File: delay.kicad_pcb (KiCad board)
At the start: 2 copper layers, 56 parts, among them J1 Footswitch_Terminal_01x02, J2 LED_Socket_01x02, J3 Footswitch_Terminal_Signal_01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, J4 Power_Supply_Terminal_01x02, J5 IO_Ground_Terminal_01x02, U1 L7805, U2 TL072, U3 PT2399

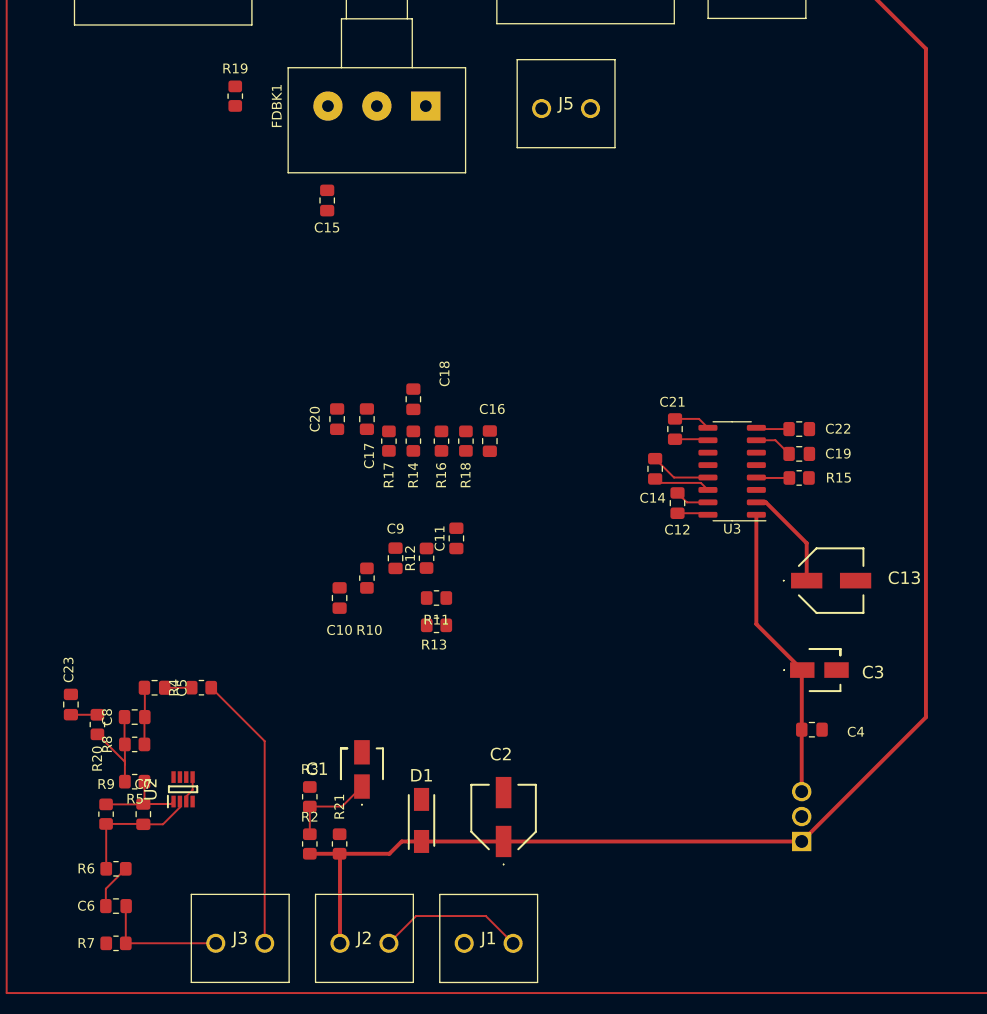
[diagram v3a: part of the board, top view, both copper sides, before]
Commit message: update pcb design schema
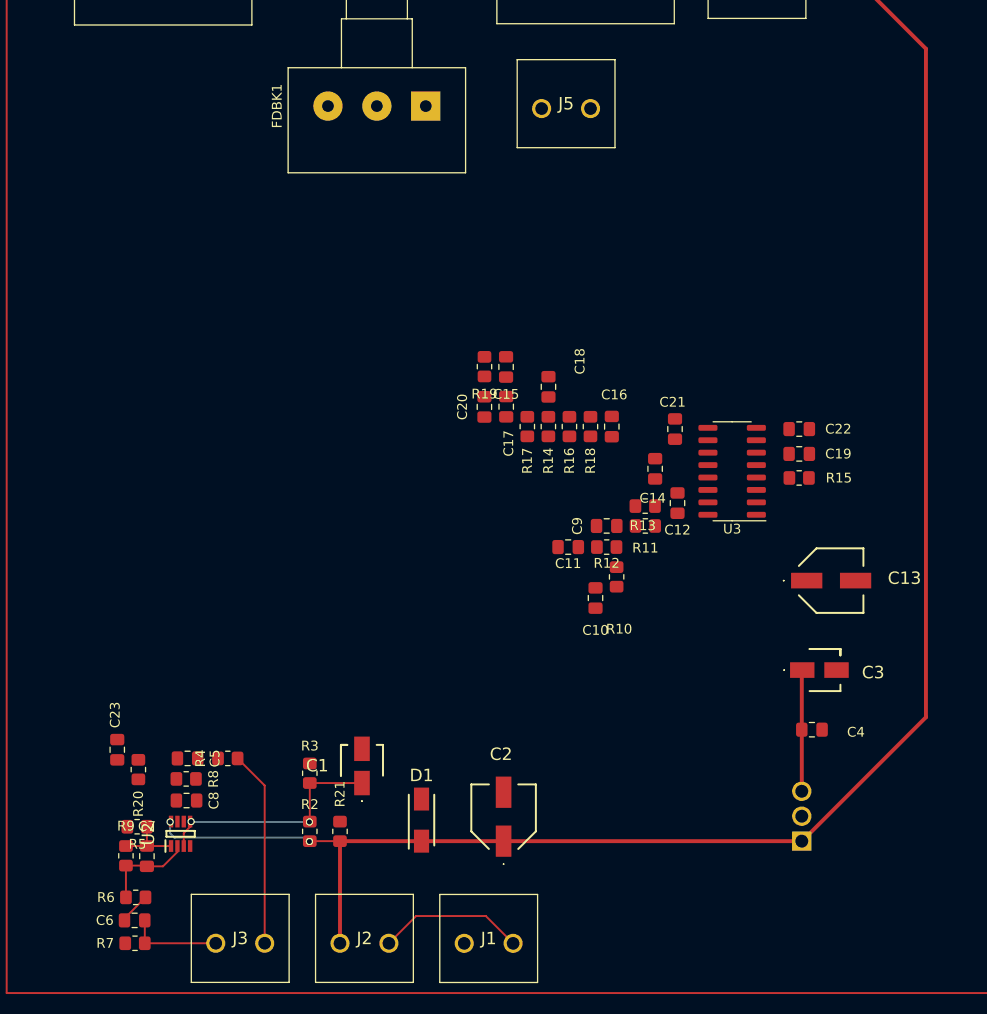
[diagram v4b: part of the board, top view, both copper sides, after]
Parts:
- moved R19 37.6 mm to (169.5, 71.9), turned to -90 degrees
- moved C10 26.2 mm to (180.8, 95.5)
- moved R10 25.5 mm to (183.0, 93.3)
- moved C15 25.0 mm to (171.7, 71.9)
- moved R13 24.6 mm to (185.9, 86.1)
- moved R11 22.6 mm to (185.9, 88.1)
- moved C9 21.8 mm to (182.0, 88.1), turned to 180 degrees
- moved R12 18.5 mm to (182.0, 90.3), turned to 180 degrees
- moved C20 15.1 mm to (169.5, 76.0)
- moved C17 14.3 mm to (171.7, 75.9)
- moved R17 14.2 mm to (173.9, 78.0)
- moved R14 13.9 mm to (176.0, 78.0)
- moved C18 13.9 mm to (176.0, 73.9)
- moved R16 13.2 mm to (178.2, 78.0)
- moved R18 12.8 mm to (180.3, 78.0)
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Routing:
- net /REG_OUT: track 30.3 -> 12.5 mm
- net /+LED: track 155.0 -> 171.5 mm, vias 0 -> 2
- net /V_B: track 12.0 -> 24.2 mm, vias 0 -> 2
- net Net-(U3-REF): track 10.7 -> 0.00 mm
- net Net-(U2B--): track 10.6 -> 0.00 mm
- net /OUTPUT: track 28.4 -> 20.0 mm
- net Net-(U3-LPF2-IN): track 6.20 -> 0.00 mm
- net Net-(C5-Pad1): track 5.89 -> 0.00 mm
- net Net-(U3-LPF2-OUT): track 5.86 -> 0.00 mm
- net Net-(U3-CC1): track 3.92 -> 0.00 mm
- net Net-(U3-OP1-OUT): track 3.74 -> 0.00 mm
- net Net-(U2A--): track 13.5 -> 9.76 mm
- net Net-(U3-LPF1-OUT): track 3.51 -> 0.00 mm
- net /INPUT: track 13.0 -> 9.60 mm
- net Net-(U3-OP1-IN): track 3.41 -> 0.00 mm
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
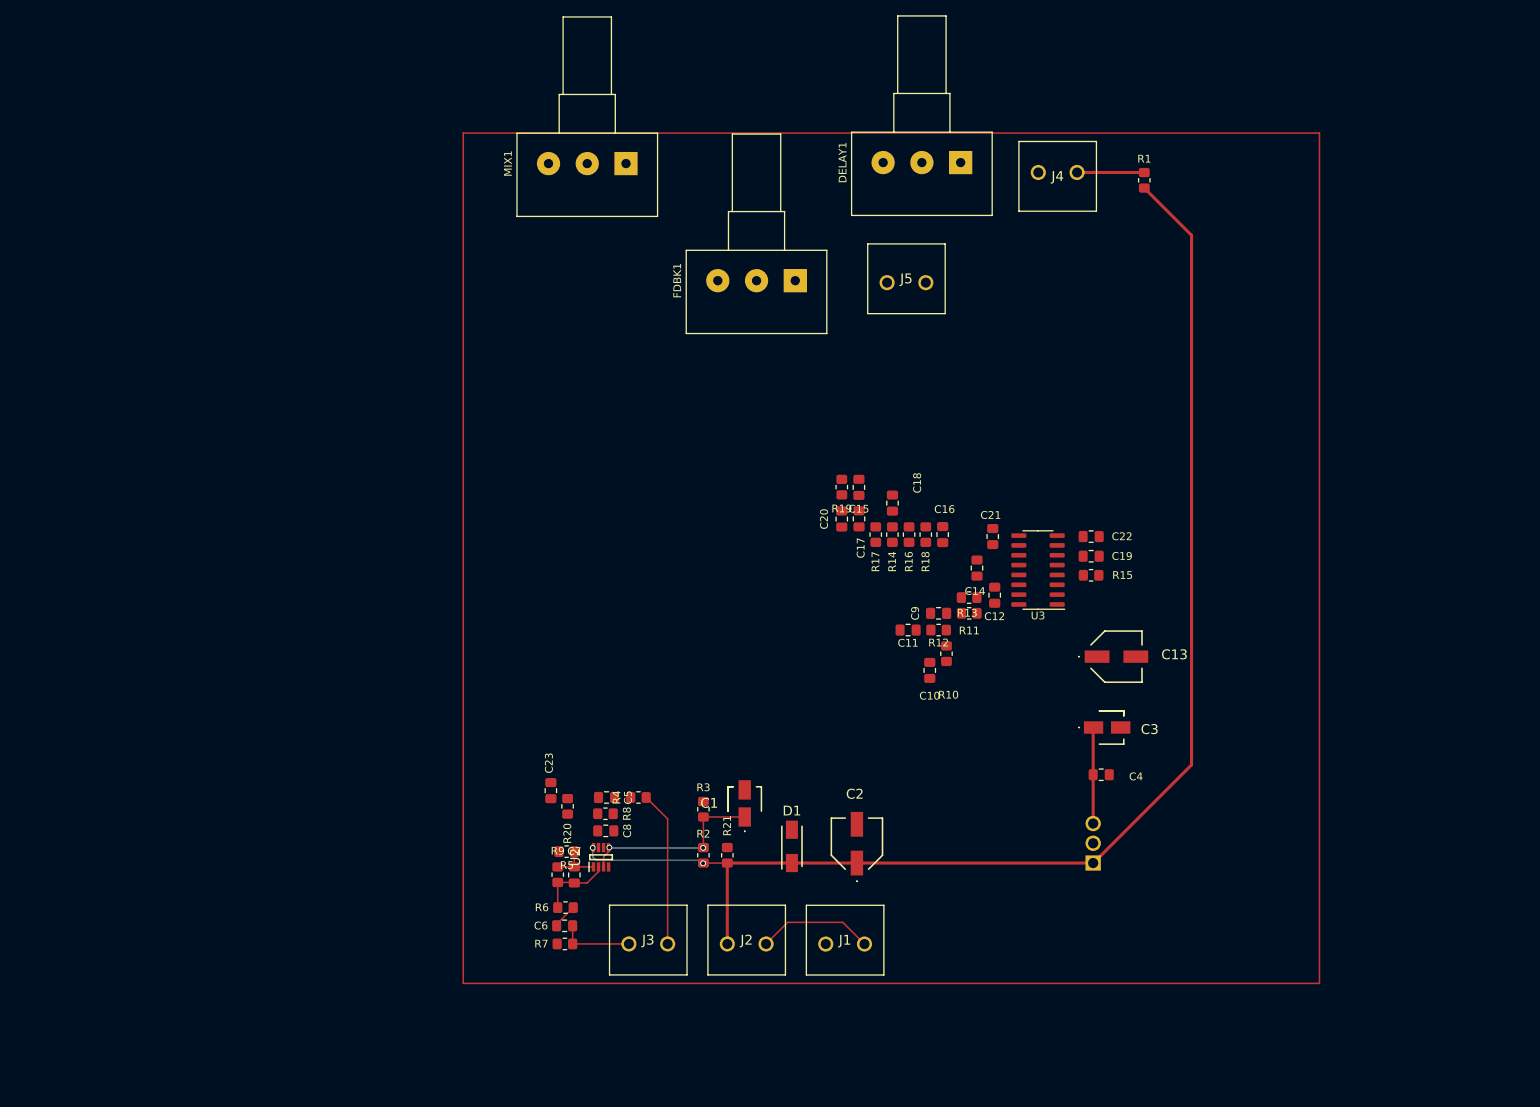
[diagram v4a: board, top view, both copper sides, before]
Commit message: create preliminary design schema with internal connections
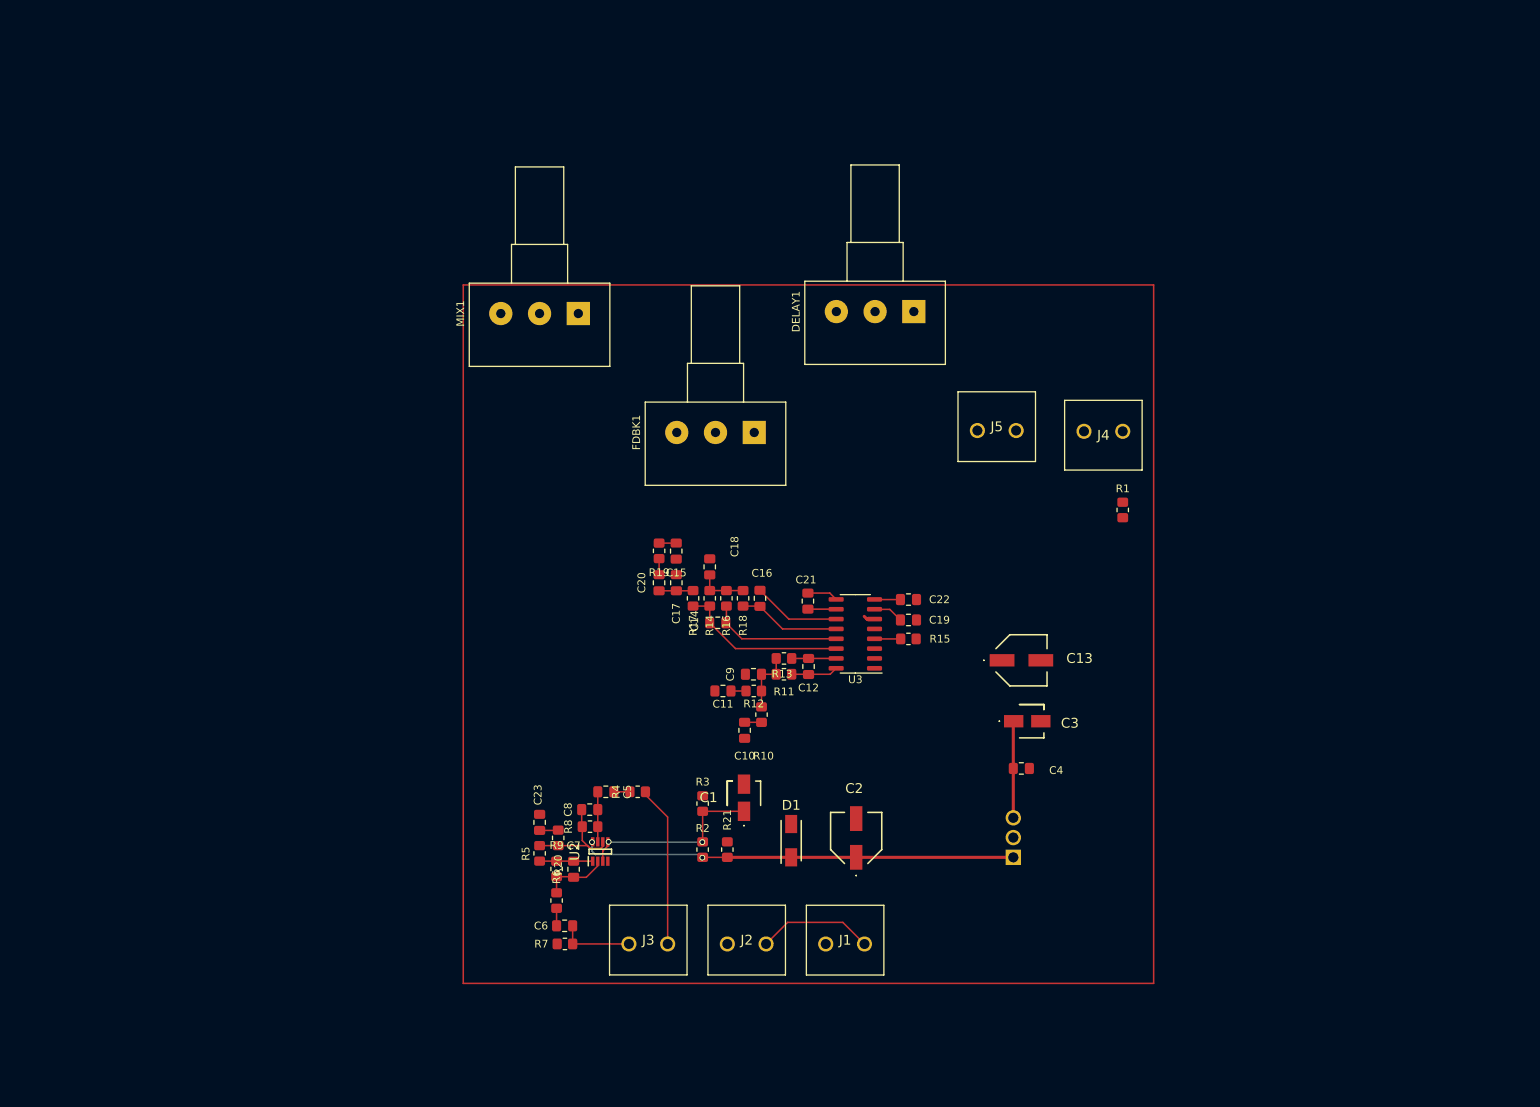
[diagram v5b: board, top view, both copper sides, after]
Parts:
- moved R1 42.6 mm to (205.8, 74.8)
- moved C14 34.2 mm to (153.5, 89.4), turned to 0 degrees
- moved J4 33.9 mm to (205.8, 64.7)
- moved C12 25.7 mm to (165.2, 95.0)
- moved C21 25.3 mm to (165.1, 86.6)
- moved R11 25.2 mm to (162.0, 96.0)
- moved C11 25.2 mm to (154.2, 98.2)
- moved C9 25.2 mm to (158.1, 96.0)
- moved R13 25.2 mm to (162.0, 94.0)
- moved R10 25.1 mm to (159.1, 101.2)
- moved R12 25.1 mm to (158.1, 98.2)
- moved C10 25.1 mm to (157.0, 103.2)
- moved C17 25.0 mm to (148.1, 84.2)
- moved C18 25.0 mm to (152.5, 82.1)
- moved U3 25.0 mm to (171.2, 90.8)
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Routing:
- net /+LED: track 171.5 -> 56.0 mm
- net Net-(U3-LPF2-OUT): track 0.00 -> 22.0 mm
- net Net-(U3-LPF2-IN): track 0.00 -> 17.3 mm
- net Net-(U2B--): track 0.00 -> 13.9 mm
- net Net-(U3-OP2-OUT): track 0.00 -> 13.2 mm
- net Net-(U3-OP2-IN): track 0.00 -> 11.4 mm
- net VDD: track 8.68 -> 0.00 mm
- net Net-(C9-Pad1): track 0.00 -> 8.15 mm
- net Net-(C5-Pad1): track 0.00 -> 6.46 mm
- net Net-(C18-Pad2): track 0.00 -> 6.33 mm
- net Net-(U3-LPF1-IN): track 0.00 -> 6.05 mm
- net Net-(U3-LPF1-OUT): track 0.00 -> 5.73 mm
- net Net-(C17-Pad2): track 0.00 -> 4.40 mm
- net Net-(U3-OP1-OUT): track 0.00 -> 3.98 mm
- net Net-(U3-CC1): track 0.00 -> 3.91 mm
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
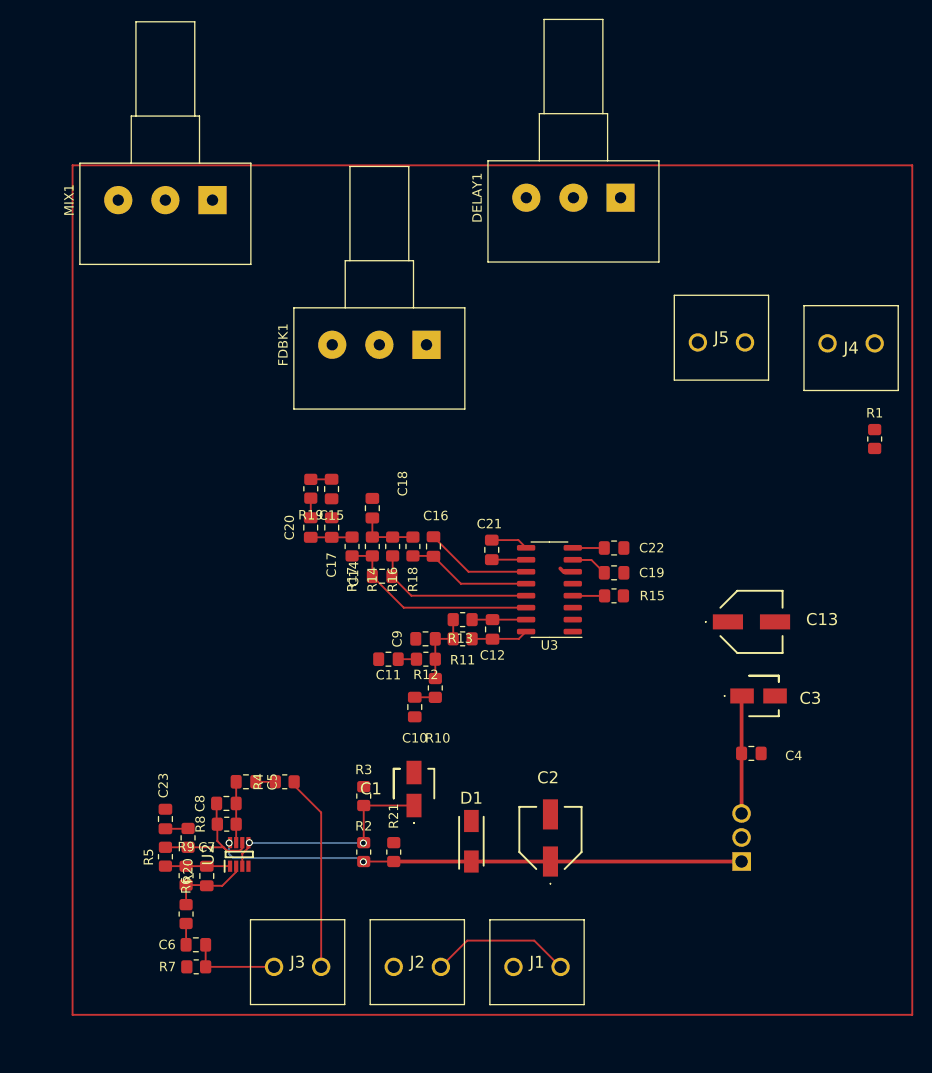
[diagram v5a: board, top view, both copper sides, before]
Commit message: create connections for all signals except 0
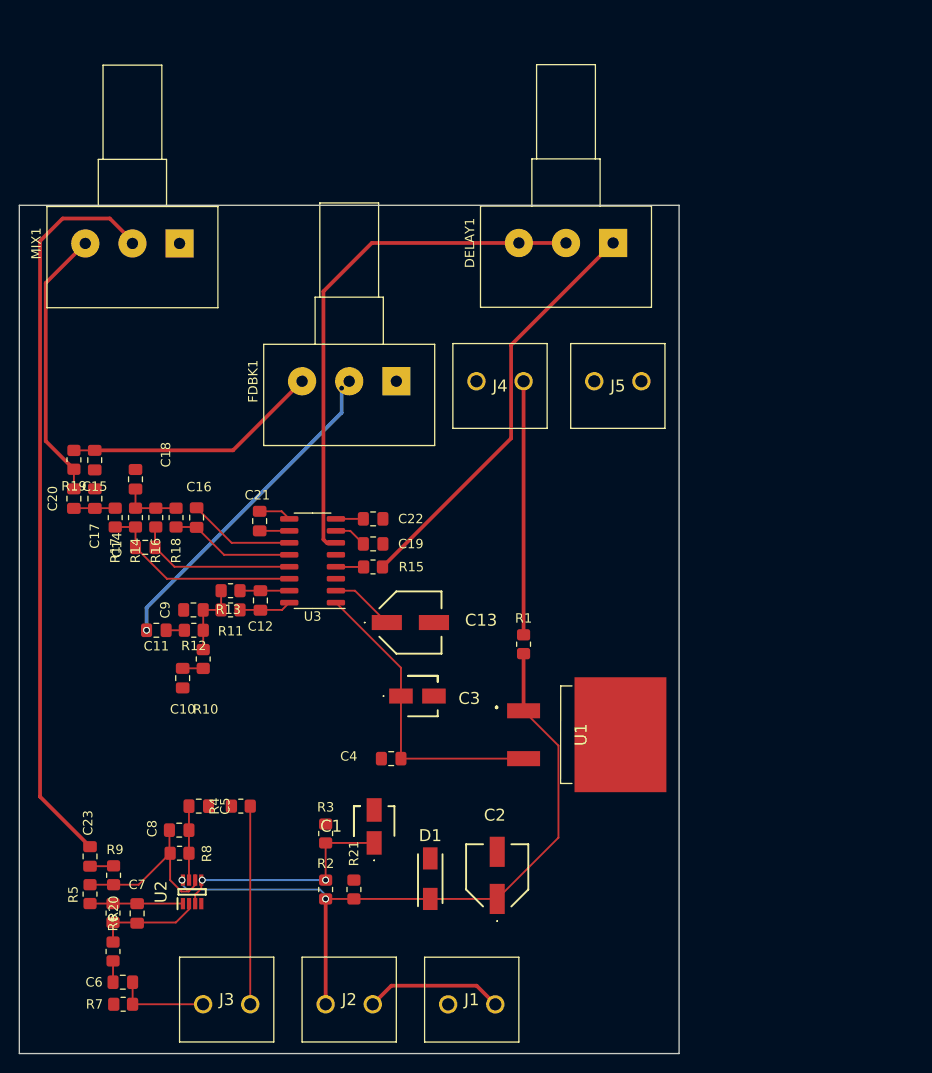
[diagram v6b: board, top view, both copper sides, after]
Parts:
- U1: footprint Ic:TO255P460X1020X2008-3P -> Ic:L7805CD2T; moved to F.Cu
- moved R1 43.1 mm to (168.5, 96.6)
- moved C4 38.2 mm to (154.5, 108.7), turned to 180 degrees
- moved J4 37.5 mm to (168.5, 68.7)
- moved C13 36.2 mm to (156.5, 94.3)
- moved C3 36.2 mm to (157.2, 102.1)
- moved C22 25.8 mm to (152.5, 83.3)
- moved C19 25.7 mm to (152.5, 85.9)
- moved R15 25.7 mm to (152.5, 88.4)
- moved C14 25.3 mm to (128.4, 86.3)
- moved C15 25.3 mm to (123.0, 77.0)
- moved C20 25.3 mm to (120.8, 81.1)
- moved C17 25.3 mm to (123.0, 81.1)
- moved C16 25.3 mm to (133.8, 83.1)
- moved C18 25.3 mm to (127.3, 79.1)
- moved R14 25.3 mm to (127.3, 83.1)
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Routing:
- net Net-(C23-Pad1): track 0.00 -> 78.5 mm
- net Net-(U3-VCO): track 1.47 -> 55.7 mm
- net Net-(DELAY1-Pad1): track 0.00 -> 44.5 mm
- net Net-(C11-Pad2): track 0.00 -> 35.4 mm, vias 0 -> 2
- net Net-(C20-Pad2): track 2.08 -> 29.0 mm
- net VDD: track 0.00 -> 26.9 mm
- net Net-(C15-Pad1): track 2.21 -> 27.2 mm
- net /+LED: track 56.0 -> 76.3 mm
- net /REG_OUT: track 12.4 -> 32.4 mm
- net Net-(U3-REF): track 0.00 -> 6.80 mm
- net Net-(U2B--): track 13.9 -> 19.3 mm
- net /SIGNAL_CLEAN: track 6.86 -> 9.86 mm
- net Net-(U2A--): track 8.63 -> 11.3 mm
- net Net-(C5-Pad2): track 2.08 -> 0.00 mm
- net Net-(C5-Pad1): track 6.46 -> 7.85 mm
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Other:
- board outline added: 70 x 90 mm
